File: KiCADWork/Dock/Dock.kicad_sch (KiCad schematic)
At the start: 2 parts, among them J1 Conn_01x10_Pin, J2 Conn_01x10_Pin

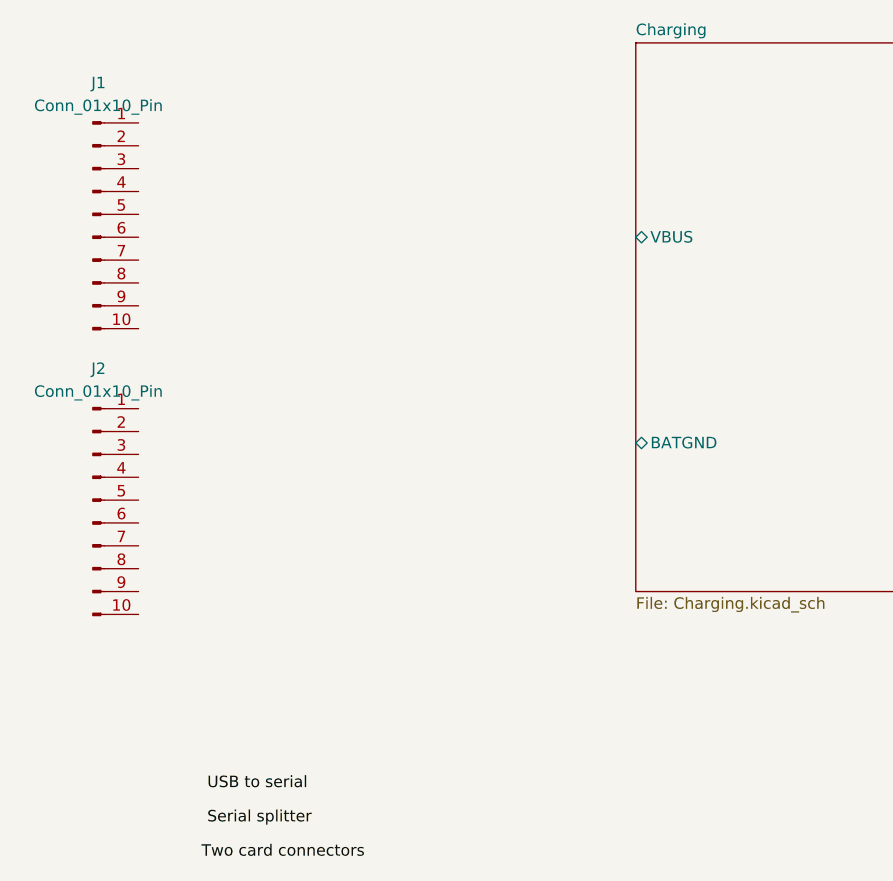
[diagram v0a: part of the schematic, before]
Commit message: New Chip NRF52833
large changes
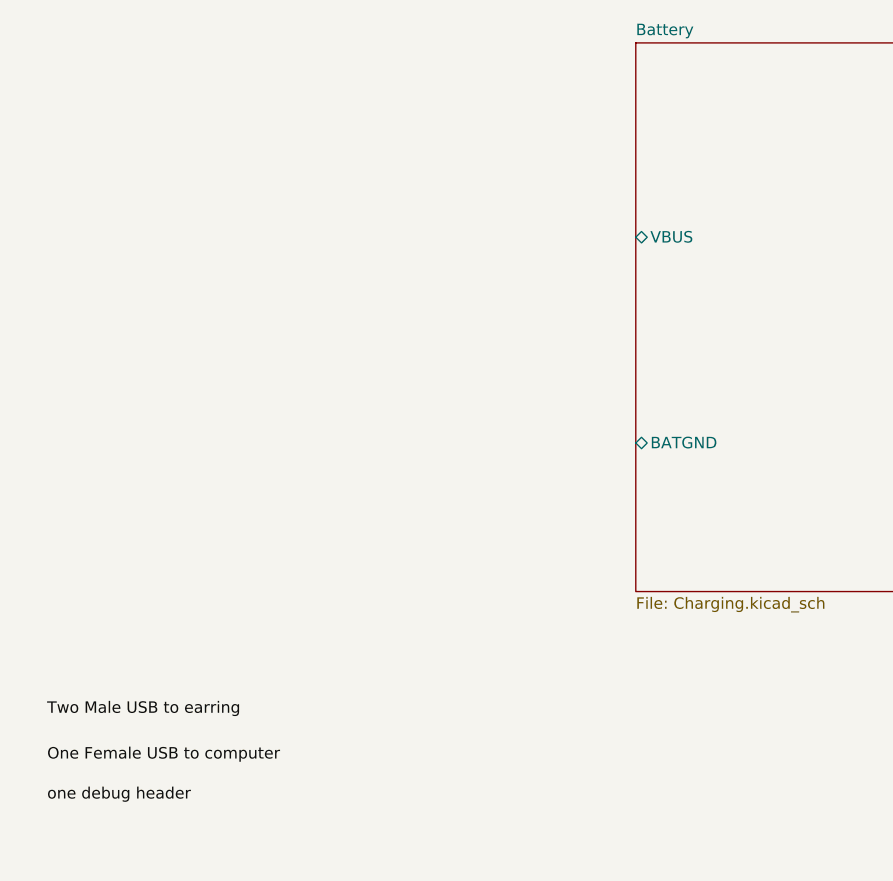
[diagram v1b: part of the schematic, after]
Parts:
- removed J1, J2: Conn_01x10_Pin, easyeda2kicad:HDR-TH_10P-P1.27-H-M-R2-C7-S1.27-W7.5-N, symbol Connector:Conn_01x10_Pin
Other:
- sheet Charging renamed Battery
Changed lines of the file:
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@@
 (kicad_sch (version 20230121) (generator eeschema)
   (paper "A4")
-  (label "Serial splitter" (at 77.47 133.35 0) (fields_autoplaced)
+  (label "Two Male USB to earring" (at 59.69 121.285 0) (fields_autoplaced)
     (effects (font (size 1.27 1.27)) (justify left bottom))
   )
-  (label "Two card connectors" (at 76.835 137.16 0) (fields_autoplaced)
+  (label "One Female USB to computer" (at 59.69 126.365 0) (fields_autoplaced)
     (effects (font (size 1.27 1.27)) (justify left bottom))
   )
-  (label "USB to serial" (at 77.47 129.54 0) (fields_autoplaced)
+  (label "one debug header" (at 59.69 130.81 0) (fields_autoplaced)
     (effects (font (size 1.27 1.27)) (justify left bottom))
-  )
-  (symbol (lib_id "Connector:Conn_01x10_Pin") (at 64.77 65.405 0) (unit 1)
-    (in_bom yes) (on_board yes) (dnp no) (fields_autoplaced)
-    (property "Reference" "J1" (at 65.405 50.8 0)
-      (effects (font (size 1.27 1.27)))
-    )
-    (property "Value" "Conn_01x10_Pin" (at 65.405 53.34 0)
-      (effects (font (size 1.27 1.27)))
-    )
-    (property "Footprint" "easyeda2kicad:HDR-TH_10P-P1.27-H-M-R2-C7-S1.27-W7.5-N" (at 64.77 65.405 0)
-      (effects (font (size 1.27 1.27)) hide)
-    )
-    (property "Datasheet" "~" (at 64.77 65.405 0)
-      (effects (font (size 1.27 1.27)) hide)
-    )
-    (pin "4")
-    (pin "9")
-    (pin "7")
-    (pin "8")
-    (pin "6")
-    (pin "2")
-    (pin "1")
-    (pin "10")
-    (pin "3")
-    (pin "5")
-    (instances
-      (project "Dock"
-        (path "/6f84fb5e-0715-49fa-a507-16643db39fa4"
-          (reference "J1") (unit 1)
-        )
-      )
-    )
-  )
-  (symbol (lib_id "Connector:Conn_01x10_Pin") (at 64.77 97.155 0) (unit 1)
-    (in_bom yes) (on_board yes) (dnp no) (fields_autoplaced)
-    (property "Reference" "J2" (at 65.405 82.55 0)
-      (effects (font (size 1.27 1.27)))
-    )
-    (property "Value" "Conn_01x10_Pin" (at 65.405 85.09 0)
-      (effects (font (size 1.27 1.27)))
-    )
-    (property "Footprint" "easyeda2kicad:HDR-TH_10P-P1.27-H-M-R2-C7-S1.27-W7.5-N" (at 64.77 97.155 0)
-      (effects (font (size 1.27 1.27)) hide)
-    )
-    (property "Datasheet" "~" (at 64.77 97.155 0)
-      (effects (font (size 1.27 1.27)) hide)
-    )
-    (pin "4")
-    (pin "9")
-    (pin "7")
-    (pin "8")
-    (pin "6")
-    (pin "2")
-    (pin "1")
-    (pin "10")
-    (pin "3")
-    (pin "5")
-    (instances
-      (project "Dock"
-        (path "/6f84fb5e-0715-49fa-a507-16643db39fa4"
-          (reference "J2") (unit 1)
-        )
-      )
-    )
   )
   (sheet (at 125.095 46.355) (size 68.58 60.96) (fields_autoplaced)
     (stroke (width 0.1524) (type solid))
     (fill (color 0 0 0 0.0000))
-    (property "Sheetname" "Charging" (at 125.095 45.6434 0)
+    (property "Sheetname" "Battery" (at 125.095 45.6434 0)
       (effects (font (size 1.27 1.27)) (justify left bottom))
     )

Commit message: Dock Updates
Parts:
- added J1: Conn_01x10_Socket, easyeda2kicad:HDR-TH_10P-P1.27_X1321FR-2X05-C43D24, symbol Connector:Conn_01x10_Socket
- added J1: USB_C_Receptacle, easyeda2kicad:TYPE-C-SMD_C9900025773, symbol Connector:USB_C_Receptacle
- added J2, J3: USB_C_Receptacle, easyeda2kicad:USB-C-SMD_TYPEC-952-ACP24, symbol Connector:USB_C_Receptacle
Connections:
- new net: J1.3 (Pin_3), J1.5 (Pin_5)
- new net DeviceSelect/D+: J1.A6 (D+), J1.B6 (D+)
- new net DeviceSelect/D-: J1.A7 (D-), J1.B7 (D-)
- new net DeviceSelect/D1+: J2.A6 (D+), J2.B6 (D+)
- new net DeviceSelect/D1-: J2.A7 (D-), J2.B7 (D-)
- new net DeviceSelect/D2+: J3.A6 (D+), J3.B6 (D+)
- new net DeviceSelect/D2-: J3.A7 (D-), J3.B7 (D-)
- new net GND: J1.A1 (GND), J1.A12 (GND), J1.B1 (GND), J1.B12 (GND), J1.S1 (SHIELD), J2.A1 (GND), J2.A12 (GND), J2.B1 (GND), J2.B12 (GND), J2.S1 (SHIELD), J3.A1 (GND), J3.A12 (GND), J3.B1 (GND), J3.B12 (GND), J3.S1 (SHIELD)
- new net SWCLK: J1.4 (Pin_4)
- new net SWDCLK: J2.A3 (TX1-), J2.B3 (TX2-), J3.A3 (TX1-), J3.B3 (TX2-)
- new net SWDIO: J1.2 (Pin_2), J2.A2 (TX1+), J2.B2 (TX2+), J3.A2 (TX1+), J3.B2 (TX2+)
- new net SWO: J2.A11 (RX2+), J2.B11 (RX1+), J3.A11 (RX2+), J3.B11 (RX1+)
- new net TDI: J1.8 (Pin_8)
- new net VTRef: J1.1 (Pin_1), J1.A4 (VBUS), J1.A9 (VBUS), J1.B4 (VBUS), J1.B9 (VBUS), J2.A4 (VBUS), J2.A9 (VBUS), J2.B4 (VBUS), J2.B9 (VBUS), J3.A4 (VBUS), J3.A9 (VBUS), J3.B4 (VBUS), J3.B9 (VBUS)
- new net nRESET: J1.10 (Pin_10), J1.6 (Pin_6), J2.A10 (RX2-), J2.B10 (RX1-), J3.A10 (RX2-), J3.B10 (RX1-)
- no-connect marks 0 -> 10
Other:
- removed sheet Battery
- added sheet DeviceSelect (DeviceSelect.kicad_sch)
- added sheet ExtraBattery (DockBattery.kicad_sch)

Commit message: Dock Updates
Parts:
- removed J2: USB_C_Receptacle, easyeda2kicad:USB-C-SMD_TYPEC-952-ACP24, symbol Connector:USB_C_Receptacle
- added P1: USB_C_Plug, easyeda2kicad:USB-C-SMD_TYPEC-952-ACP24, symbol Connector:USB_C_Plug
- added R1 (x2): 5k1, Resistor_SMD:R_0402_1005Metric_Pad0.72x0.64mm_HandSolder, symbol Device:R
- J1: footprint easyeda2kicad:HDR-TH_10P-P1.27_X1321FR-2X05-C43D24 -> easyeda2kicad:HDR-TH_10P-P1.27-V-M-R2-C5-S1.27-1
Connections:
- net DeviceSelect/D- is gone; now on net DeviceSelect/D+: J1.A7 (D-), J1.B7 (D-)
- net DeviceSelect/D+: now also J1.B10 (RX1-), J1.B11 (RX1+)
- net DeviceSelect/D1+: now also P1.A6 (D+)
- net DeviceSelect/D1-: now also P1.A7 (D-)
- net GND: now also P1.A1 (GND), P1.A12 (GND), P1.B1 (GND), P1.B12 (GND), P1.S1 (SHIELD), R1.1, R1.1
- net SWDCLK: now also P1.A3 (TX1-), P1.B3 (TX2-)
- net SWDIO: now also P1.A2 (TX1+), P1.B2 (TX2+)
- net SWO: now also P1.A11 (RX2+), P1.B11 (RX1+)
- net VTRef: no longer J3.A4 (VBUS), J3.A9 (VBUS), J3.B4 (VBUS), J3.B9 (VBUS)
- net nRESET: now also P1.A10 (RX2-), P1.B10 (RX1-)
- net at J1.A5 (CC1): now also R1.2
- net at J1.B5 (CC2): now also R1.2
- new net DeviceSelect/VBUS1: P1.A4 (VBUS), P1.A9 (VBUS), P1.B4 (VBUS), P1.B9 (VBUS)
- new net DeviceSelect/VBUS2: J3.A4 (VBUS), J3.A9 (VBUS), J3.B4 (VBUS), J3.B9 (VBUS)
- no-connect marks 10 -> 20
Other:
- sheet DeviceSelect ports: added VBUS1, VBUS2, VBus; removed none
- sheet ExtraBattery ports: added VBAT, VBUS; removed none
- moved on the sheet: J1

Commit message: Ignoring Backups
More Dock progress
All local backups removed
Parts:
- removed J3: USB_C_Receptacle, easyeda2kicad:USB-C-SMD_TYPEC-952-ACP24, symbol Connector:USB_C_Receptacle
- added P2: USB_C_Plug, easyeda2kicad:USB-C-SMD_918-118A2021S40003, symbol Connector:USB_C_Plug
- J1: LCSC Part (none) -> C2935953
- J1: LCSC Part (none) -> C5156605
- P1: footprint easyeda2kicad:USB-C-SMD_TYPEC-952-ACP24 -> easyeda2kicad:USB-C-SMD_918-118A2021S40003; LCSC Part (none) -> C2763095
- R1: LCSC Part (none) -> C105872
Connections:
- net DeviceSelect/D2+: now also P2.A6 (D+)
- net DeviceSelect/D2-: now also P2.A7 (D-)
- net DeviceSelect/VBUS2: now also P2.A4 (VBUS), P2.A9 (VBUS), P2.B4 (VBUS), P2.B9 (VBUS)
- net GND: now also P2.A1 (GND), P2.A12 (GND), P2.B1 (GND), P2.B12 (GND), P2.S1 (SHIELD)
- net SWDCLK: now also P2.A3 (TX1-), P2.B3 (TX2-)
- net SWDIO: now also P2.A2 (TX1+), P2.B2 (TX2+)
- net SWO: now also P2.A11 (RX2+), P2.B11 (RX1+)
- net nRESET: now also P2.A10 (RX2-), P2.B10 (RX1-)
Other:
- sheet DeviceSelect ports: added Vsys; removed VBus
- sheet ExtraBattery ports: added Vsys; removed VBAT

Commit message: Beautiful Skilkscreen Added
Dock schematic intial draft complete
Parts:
- added TP1, TP11, TP12, TP13, TP14, TP15, TP16, TP17, TP2: TestPoint, TestPoint:TestPoint_Pad_D1.0mm, symbol Connector:TestPoint
- R1: LCSC Part C105872 -> C103086
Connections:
- net DeviceSelect/VBUS1: now also TP1.1
- net DeviceSelect/VBUS2: now also TP2.1
- net SWCLK: now also TP13.1
- net SWDIO: now also TP12.1
- net TDI: now also TP15.1
- net VTRef: now also TP11.1
- net nRESET: now also TP14.1, TP16.1
- net at J1.3 (Pin_3), J1.5 (Pin_5): now also TP17.1

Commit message: Small Updates
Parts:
- P1, P2: footprint easyeda2kicad:USB-C-SMD_918-118A2021S40003 -> easyeda2kicad:USB-C-SMD_TYPE-C-24P-GTJB-040
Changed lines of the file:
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@@
+    (effects (font (size 1.27 1.27)) (justify left bottom))
+  )
+  (label "Earrings do not check the CC connection" (at 151.765 153.67 0) (fields_autoplaced)
     (effects (font (size 1.27 1.27)) (justify left bottom))
   )
@@
       (effects (font (size 1.27 1.27)))
     )
-    (property "Footprint" "easyeda2kicad:USB-C-SMD_918-118A2021S40003" (at 229.235 113.665 0)
+    (property "Footprint" "easyeda2kicad:USB-C-SMD_TYPE-C-24P-GTJB-040" (at 229.235 113.665 0)
       (effects (font (size 1.27 1.27)) hide)
     )
@@
       (effects (font (size 1.27 1.27)))
     )
-    (property "Footprint" "easyeda2kicad:USB-C-SMD_918-118A2021S40003" (at 261.62 46.99 0)
-      (effects (font (size 1.27 1.27)) hide)
-    )
+    (property "Footprint" "easyeda2kicad:USB-C-SMD_TYPE-C-24P-GTJB-040" (at 261.62 46.99 0)
+      (effects (font (size 1.27 1.27)) hide)
+    )
